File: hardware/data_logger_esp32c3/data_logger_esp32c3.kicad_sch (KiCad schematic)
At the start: 42 parts, among them U1 ESP32-C3-MINI-1, U3 LM321MF, U4 LM321MF, U5 LM321MF, U6 LM321MF, U7 LM321MF, U8 LM321MF

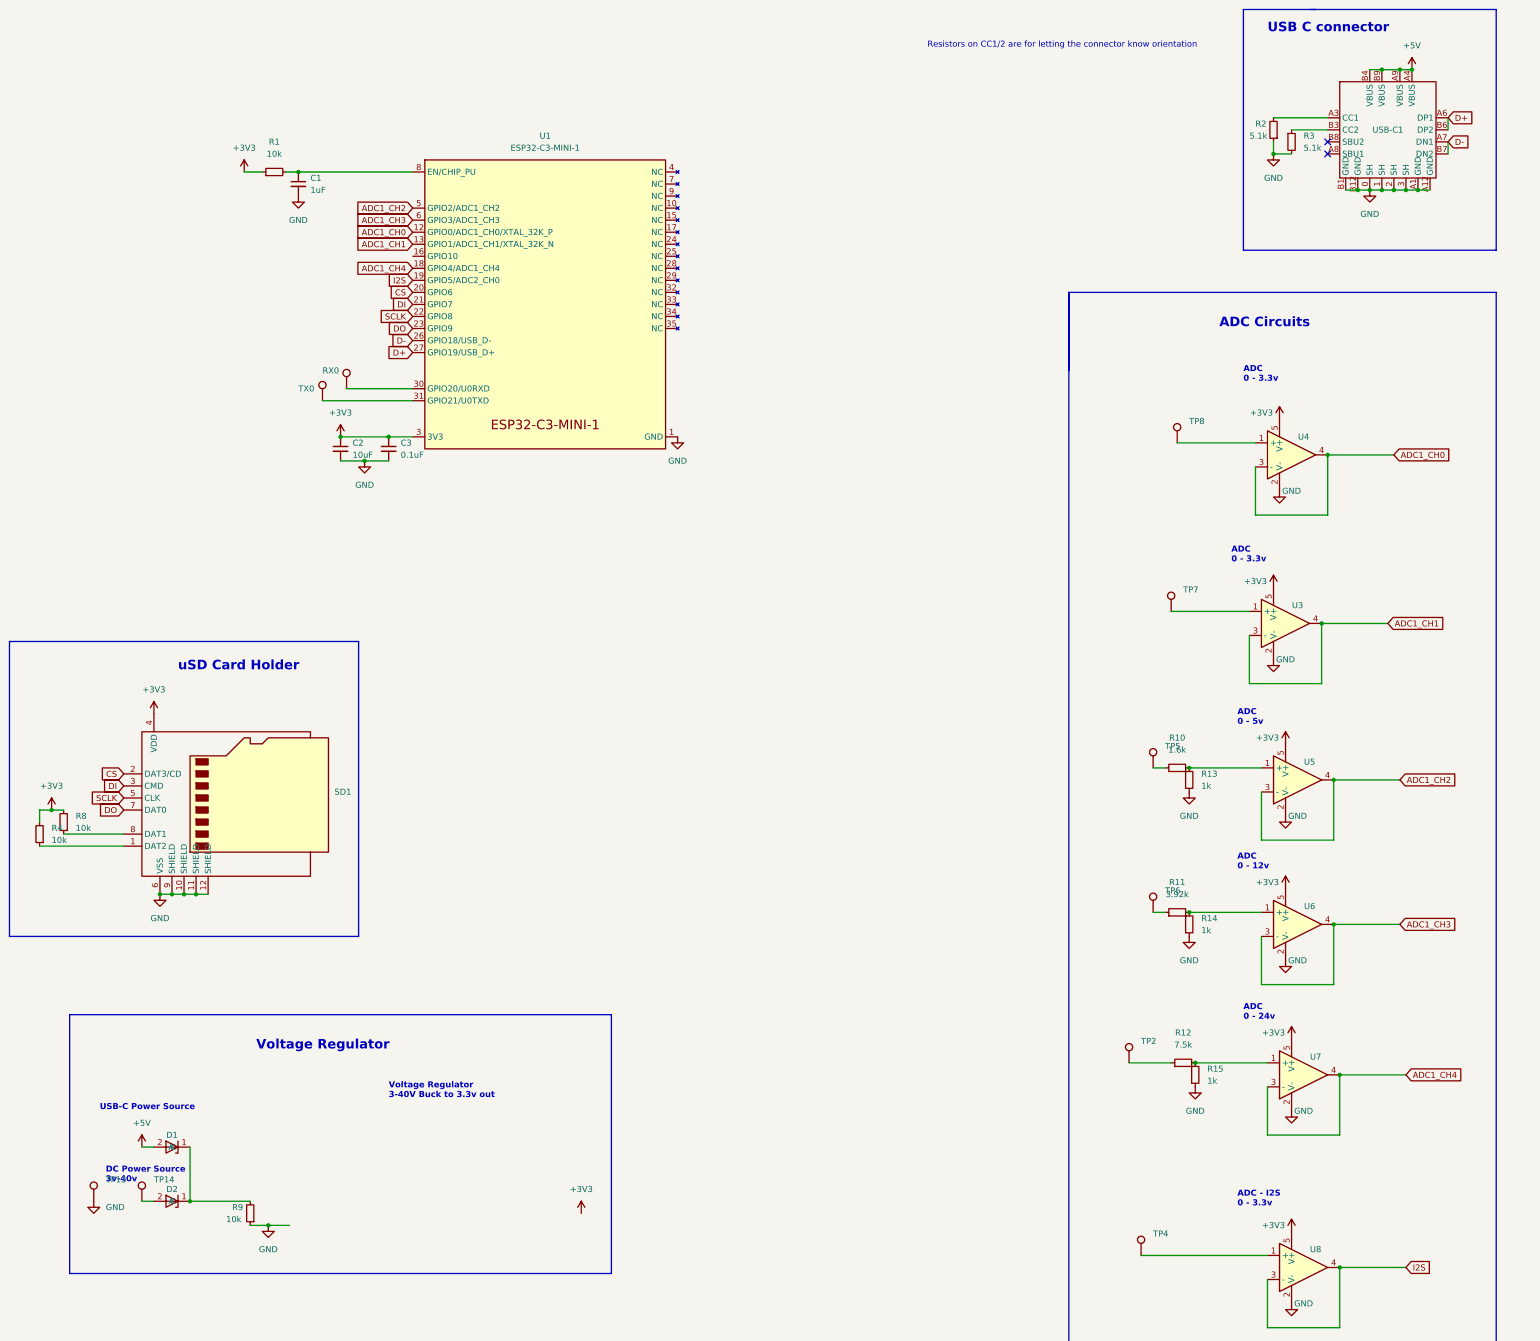
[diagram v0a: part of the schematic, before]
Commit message: added linear regulator, changed to 0402 passives
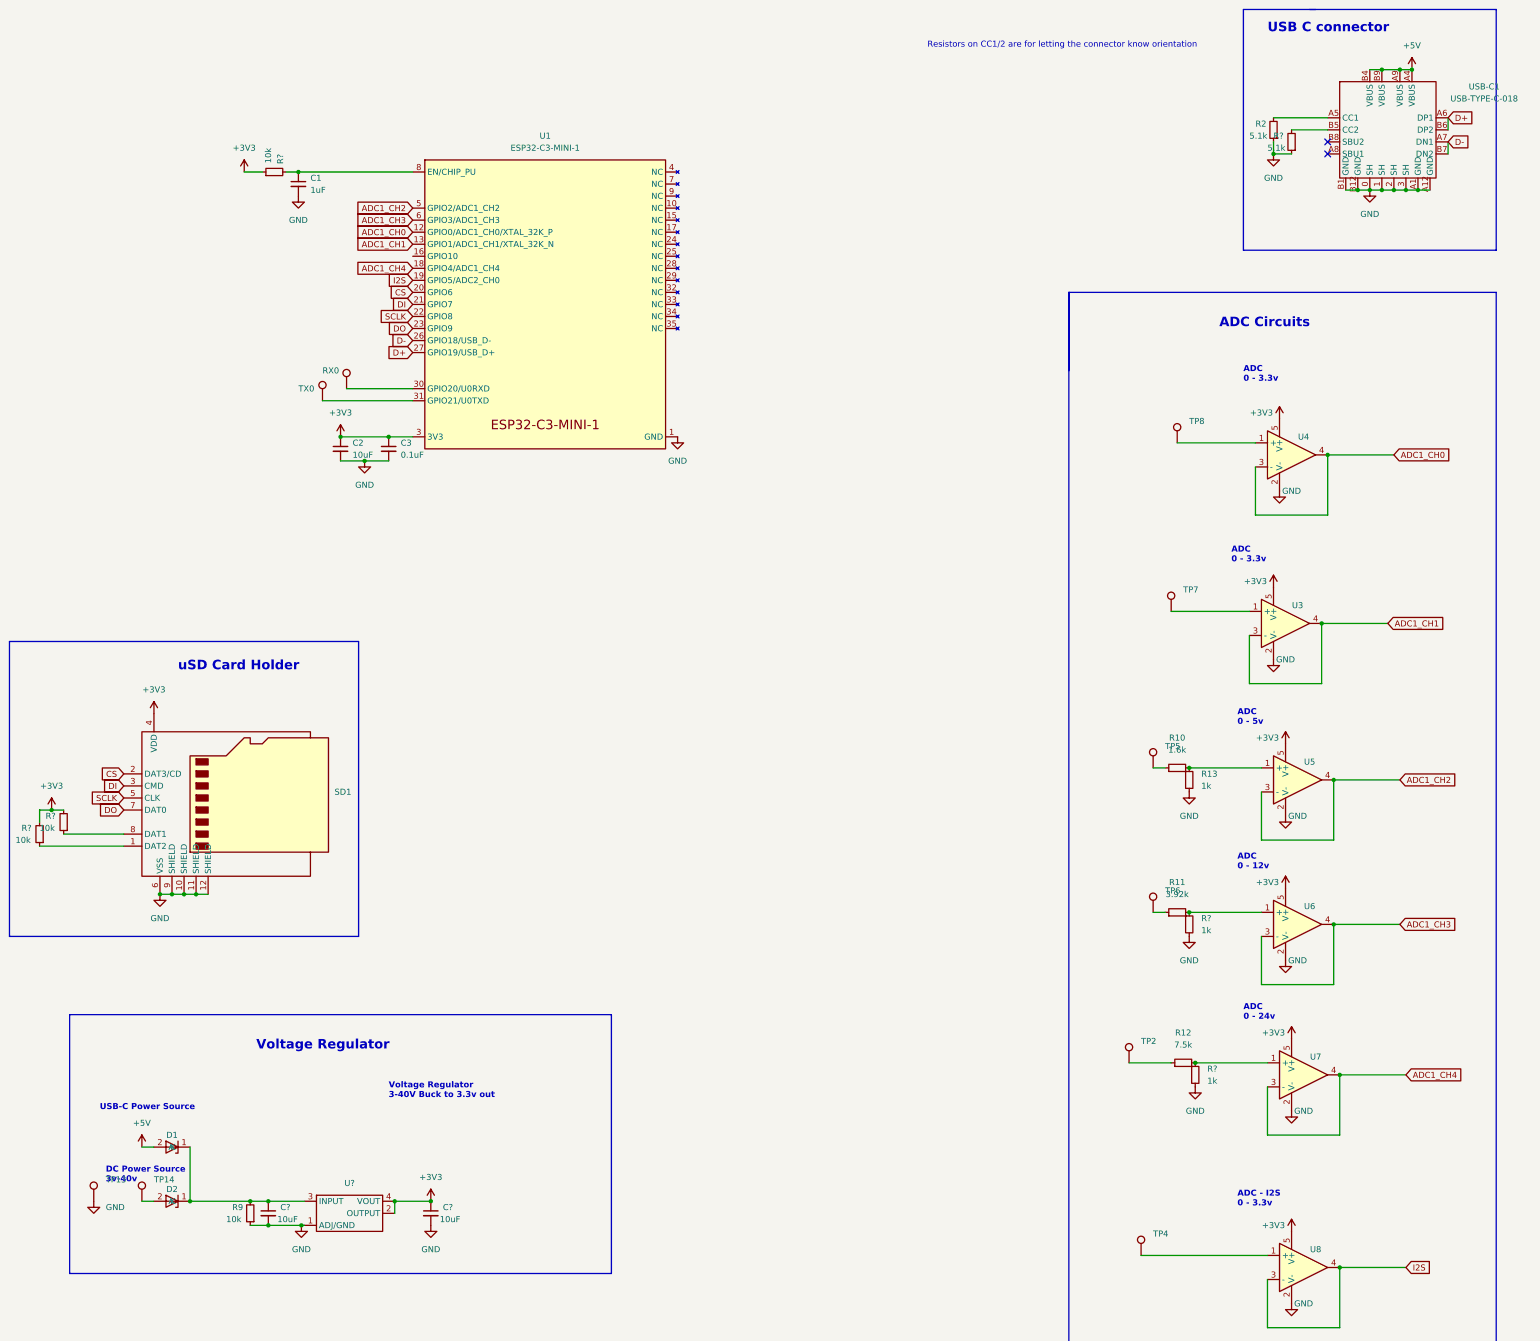
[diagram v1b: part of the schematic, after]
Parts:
- removed R1, R4, R8: 10k, Resistor_SMD:R_0603_1608Metric, symbol Device:R_Small
- removed R14, R15: 1k, Resistor_SMD:R_0603_1608Metric, symbol Device:R_Small
- removed R3: 5.1k, Resistor_SMD:R_0603_1608Metric, symbol Device:R_Small
- removed USB-C1: USB-TYPE-C-018, lib:USB-TYPE-C-018, symbol lib:USB-TYPE-C-018
- added C? (x2): 10uF, Capacitor_SMD:C_0603_1608Metric, symbol Device:C_Small
- added R? (x3): 10k, Resistor_SMD:R_0402_1005Metric, symbol Device:R_Small
- added R?: 5.1k, Resistor_SMD:R_0402_1005Metric, symbol Device:R_Small
- added R? (x2): 1k, Resistor_SMD:R_0402_1005Metric, symbol Device:R_Small
- added U?: AZ1117IH-3.3TRG1, symbol 1_project_specific:AZ1117IH-3.3TRG1
- added USB-C1: USB-TYPE-C-018, lib:USB-TYPE-C-018, symbol 1_project_specific:USB-TYPE-C-018
- R10: footprint Resistor_SMD:R_0603_1608Metric -> Resistor_SMD:R_0402_1005Metric; part_number RC-02W1601FT -> RMC04021.6K1%N
- R11: footprint Resistor_SMD:R_0603_1608Metric -> Resistor_SMD:R_0402_1005Metric; part_number ERJ3EKF3921V -> RC0402FR-073K9L
- R12: footprint Resistor_SMD:R_0603_1608Metric -> Resistor_SMD:R_0402_1005Metric; part_number C114634 -> AECR0402F7K50K9
- R13: footprint Resistor_SMD:R_0603_1608Metric -> Resistor_SMD:R_0402_1005Metric; part_number RS-03K102JT -> CR-02FL6----1K
- R2: footprint Resistor_SMD:R_0603_1608Metric -> Resistor_SMD:R_0402_1005Metric; part_number RC0603FR-075K1L -> ERJ2RKF5101X
- R9: footprint Resistor_SMD:R_0603_1608Metric -> Resistor_SMD:R_0402_1005Metric; part_number AC0603FR-0710KL -> ERJ2RKF1002X
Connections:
- net +3V3: now also C?.1, R?.1, R?.2, R?.2, U?.2 (OUTPUT), U?.4 (VOUT)
- net +5V: now also USB-C1.A4 (VBUS), USB-C1.A9 (VBUS), USB-C1.B4 (VBUS), USB-C1.B9 (VBUS)
- net D+: now also USB-C1.A6 (DP1), USB-C1.B6 (DP2)
- net D-: now also USB-C1.A7 (DN1), USB-C1.B7 (DN2)
- net GND: now also C?.2, C?.2, R?.1, R?.2, R?.2, U?.1 (ADJ/GND), USB-C1.0 (SH), USB-C1.1 (SH), USB-C1.2 (SH), USB-C1.3 (SH), USB-C1.A1 (GND), USB-C1.A12 (GND), USB-C1.B1 (GND), USB-C1.B12 (GND)
- net at R2.2: now also USB-C1.A5 (CC1)
- net at R12.2, U7.1 (+): now also R?.1
- net at D1.1 (K), D2.1 (K), R9.2: now also C?.1, U?.3 (INPUT)
- net at R11.2, U6.1 (+): now also R?.1
- net at SD1.1 (DAT2): now also R?.1
- net at SD1.8 (DAT1): now also R?.1
- net at C1.1, U1.8 (EN/CHIP_PU): now also R?.2
- new net: R?.2, USB-C1.B5 (CC2)

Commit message: Adding to pcb
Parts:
- removed C? (x2): 10uF, Capacitor_SMD:C_0603_1608Metric, symbol Device:C_Small
- removed D1, D2: B0530WS_SE, lib:B0530WS_SE, symbol lib:B0530WS_SE
- removed TP1, TP10, TP11, TP12, TP13, TP14, TP2, TP3, TP4, TP5, TP6, TP7, TP8, TP9: TestPoint, TestPoint:TestPoint_Loop_D2.50mm_Drill1.0mm, symbol Connector:TestPoint
- added 3V3, ADC1+1, ADC1-1, ADC2+1, ADC2-1, ADC3+1, ADC3-1, ADC4+1, ADC4-1, ADC5+1, ADC5-1, ADC6+1, ADC6-1, DC+1, DC-1, VIN1: TestPoint, TestPoint:TestPoint_THTPad_1.0x1.0mm_Drill0.5mm, symbol Connector:TestPoint
- added C4, C5: 10uF, Capacitor_SMD:C_0603_1608Metric, symbol Device:C_Small
- added D1: LTVS16H5.0T5G, 1_project_footprints:DFN1610, symbol 1_project_specific:LTVS16H5.0T5G
- added U10, U9: A03401A, 1_project_footprints:SOT-23, symbol 1_project_specific:A03401A
- C1: footprint Capacitor_SMD:C_0603_1608Metric -> Capacitor_SMD:C_0402_1005Metric; part_number TMK107AB7105KAHT -> 0402X105K6R3NT
- C2: part_number GRM188R61A106ME69D -> CL10A106KO8NQNC
- C3: footprint Capacitor_SMD:C_0603_1608Metric -> Capacitor_SMD:C_0402_1005Metric; part_number AC0603KRX7R9BB104 -> GCM155L81E104KE02D
- RX0, TX0: footprint TestPoint:TestPoint_Loop_D2.50mm_Drill1.0mm -> TestPoint:TestPoint_THTPad_1.0x1.0mm_Drill0.5mm
- SD1: footprint lib:472192001 -> 1_project_footprints:472192001
- U1: footprint Espressif:ESP32-C3-MINI-1 -> 1_espressif:ESP32-C3-MINI-1
- U2: renamed from U?; footprint (none) -> 1_project_footprints:SOT-223-4
- U3, U4, U5, U6, U7, U8: footprint lib:LM321MF -> 1_project_footprints:LM321MF
- USB-C1: footprint lib:USB-TYPE-C-018 -> 1_project_footprints:USB-TYPE-C-018
- gave numbers to parts that had none: 6
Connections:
- net +3V3: now also 3V3.1, C5.1
- net +5V: now also U10.3 (D)
- net GND: now also ADC1-1.1, ADC2-1.1, ADC3-1.1, ADC4-1.1, ADC5-1.1, ADC6-1.1, C4.2, C5.2, D1.2 (A), DC-1.1, U10.1 (G), U9.1 (G)
- net at U3.1 (+): now also ADC2+1.1
- net at R10.1: now also ADC3+1.1
- net at R11.1: now also ADC4+1.1
- net at U4.1 (+): now also ADC1+1.1
- net at R12.1: now also ADC5+1.1
- net at R9.2, U2.3 (INPUT): now also C4.1, U10.2 (S), U9.2 (S), VIN1.1
- net at U8.1 (+): now also ADC6+1.1
- new net: D1.1 (K), DC+1.1, U9.3 (D)
- no-connect marks 2 -> 3
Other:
- note added: "DC Source"
- note added: "Linear Voltage Regulator"
- note removed: "DC Power Source 3v-40v"
- note removed: "Voltage Regulator"
- note removed: "Voltage Regulator 3-40V Buck to 3.3v out"
- moved on the sheet: R10, R11, R12, R13, R5, R6, U4

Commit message: More hardware work
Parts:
- removed U1: ESP32-C3-MINI-1, 1_espressif:ESP32-C3-MINI-1, symbol Espressif:ESP32-C3-MINI-1
- added U1: ESP32-C3-MINI-1, 1_espressif:ESP32-C3-MINI-1, symbol 1_espressif:ESP32-C3-MINI-1
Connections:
- net +3V3: now also U1.3 (3V3)
- net ADC1_CH0: now also U1.12 (GPIO0/ADC1_CH0/XTAL_32K_P)
- net ADC1_CH1: now also U1.13 (GPIO1/ADC1_CH1/XTAL_32K_N)
- net ADC1_CH2: now also U1.5 (GPIO2/ADC1_CH2)
- net ADC1_CH3: now also U1.6 (GPIO3/ADC1_CH3)
- net ADC1_CH4: now also U1.18 (GPIO4/ADC1_CH4)
- net CS: now also U1.20 (GPIO6)
- net D+: now also U1.27 (GPIO19/USB_D+)
- net D-: now also U1.26 (GPIO18/USB_D-)
- net DI: now also U1.21 (GPIO7)
- net DO: now also U1.23 (GPIO9)
- net GND: now also U1.1 (GND), U1.11, U1.14, U1.2 (GND), U1.36 (GND), U1.37 (GND), U1.38 (GND), U1.39 (GND), U1.40 (GND), U1.41 (GND), U1.42 (GND), U1.43 (GND), U1.44 (GND), U1.45 (GND), U1.46 (GND), U1.47 (GND), U1.48 (GND), U1.49 (GND), U1.50 (GND), U1.51 (GND), U1.52 (GND), U1.53 (GND)
- net I2S: now also U1.19 (GPIO5/ADC2_CH0)
- net SCLK: now also U1.22 (GPIO8)
- net at C1.1, R4.2: now also U1.8 (EN/CHIP_PU)
- net at RX0.1: now also U1.30 (GPIO20/U0RXD)
- net at TX0.1: now also U1.31 (GPIO21/U0TXD)
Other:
- note added: "MCU"
- note removed: "Resistors on CC1/2 are for letting the connector know orientation"

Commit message: adding to hardware
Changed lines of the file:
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@@
-    (pin "1")
-  )
-  (symbol (lib_id "Connector:TestPoint") (at 50.8 270.51 0) (unit 1)
-    (in_bom yes) (on_board yes)
-    (property "Reference" "DC+1" (id 0) (at 50.8 265.43 0)
-      (effects (font (size 1.27 1.27)) (justify left))
-    )
-    (property "Value" "TestPoint" (id 1) (at 53.34 268.4779 0)
-      (effects (font (size 1.27 1.27)) (justify left) hide)
-    )
-    (property "Footprint" "TestPoint:TestPoint_THTPad_1.0x1.0mm_Drill0.5mm" (id 2) (at 55.88 270.51 0)
-      (effects (font (size 1.27 1.27)) hide)
-    )
-    (property "Datasheet" "~" (id 3) (at 55.88 270.51 0)
-      (effects (font (size 1.27 1.27)) hide)
-    )
     (pin "1")
   )
@@
     (pin "1")
   )
+  (symbol (lib_id "Connector:TestPoint") (at 468.63 238.125 0) (unit 1)
+    (in_bom yes) (on_board yes)
+    (property "Reference" "ADC5-1" (id 0) (at 467.995 232.41 0)
+      (effects (font (size 1.27 1.27)) (justify left))
+    )
+    (property "Value" "TestPoint" (id 1) (at 471.17 236.0929 0)
+      (effects (font (size 1.27 1.27)) (justify left) hide)
+    )
+    (property "Footprint" "TestPoint:TestPoint_THTPad_1.0x1.0mm_Drill0.5mm" (id 2) (at 473.71 238.125 0)
+      (effects (font (size 1.27 1.27)) hide)
+    )
+    (property "Datasheet" "~" (id 3) (at 473.71 238.125 0)
+      (effects (font (size 1.27 1.27)) hide)
+    )
+    (pin "1")
+  )
   (symbol (lib_id "Connector:TestPoint") (at 40.64 270.51 0) (unit 1)
     (in_bom yes) (on_board yes)
-    (property "Reference" "DC-1" (id 0) (at 39.37 265.43 0)
+    (property "Reference" "DC-1" (id 0) (at 40.005 265.43 0)
       (effects (font (size 1.27 1.27)) (justify left))
     )
@@
     )
     (property "Datasheet" "~" (id 3) (at 45.72 270.51 0)
-      (effects (font (size 1.27 1.27)) hide)
-    )
-    (pin "1")
-  )
-  (symbol (lib_id "Connector:TestPoint") (at 468.63 238.125 0) (unit 1)
-    (in_bom yes) (on_board yes)
-    (property "Reference" "ADC5-1" (id 0) (at 467.995 232.41 0)
-      (effects (font (size 1.27 1.27)) (justify left))
-    )
-    (property "Value" "TestPoint" (id 1) (at 471.17 236.0929 0)
-      (effects (font (size 1.27 1.27)) (justify left) hide)
-    )
-    (property "Footprint" "TestPoint:TestPoint_THTPad_1.0x1.0mm_Drill0.5mm" (id 2) (at 473.71 238.125 0)
-      (effects (font (size 1.27 1.27)) hide)
-    )
-    (property "Datasheet" "~" (id 3) (at 473.71 238.125 0)
       (effects (font (size 1.27 1.27)) hide)
     )
@@
     (pin "1")
   )
+  (symbol (lib_id "Connector:TestPoint") (at 50.8 270.51 0) (unit 1)
+    (in_bom yes) (on_board yes)
+    (property "Reference" "DC+1" (id 0) (at 50.165 265.43 0)
+      (effects (font (size 1.27 1.27)) (justify left))
+    )
+    (property "Value" "TestPoint" (id 1) (at 53.34 268.4779 0)
+      (effects (font (size 1.27 1.27)) (justify left) hide)
+    )
+    (property "Footprint" "TestPoint:TestPoint_THTPad_1.0x1.0mm_Drill0.5mm" (id 2) (at 55.88 270.51 0)
+      (effects (font (size 1.27 1.27)) hide)
+    )
+    (property "Datasheet" "~" (id 3) (at 55.88 270.51 0)
+      (effects (font (size 1.27 1.27)) hide)
+    )
+    (pin "1")
+  )
   (symbol (lib_id "power:GND") (at 509.27 116.84 0) (unit 1)
     (in_bom yes) (on_board yes)
@@
       (reference "D1") (unit 1) (value "LTVS16H5.0T5G") (footprint "1_project_footprints:DFN1610")
     )
-    (path "/4b2a0f39-8828-4267-950c-fe5adc6b96ac"
+    (path "/ca03cb07-5523-4de3-accf-b5e1342ff21a"
       (reference "DC+1") (unit 1) (value "TestPoint") (footprint "TestPoint:TestPoint_THTPad_1.0x1.0mm_Drill0.5mm")
     )
-    (path "/b8114865-64b9-4b79-b52d-fcdd217c92d8"
+    (path "/bbe5e08f-c4ee-43f4-9366-05d99dc3ae4e"
       (reference "DC-1") (unit 1) (value "TestPoint") (footprint "TestPoint:TestPoint_THTPad_1.0x1.0mm_Drill0.5mm")
     )

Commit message: Add gpio expander.  Layout complete
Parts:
- removed ADC2+1, ADC2-1: TestPoint, TestPoint:TestPoint_THTPad_1.0x1.0mm_Drill0.5mm, symbol Connector:TestPoint
- removed U3: LM321MF, 1_project_footprints:LM321MF, symbol lib:LM321MF
- added C6, C7: 0.1uF, Capacitor_SMD:C_0402_1005Metric, symbol Device:C_Small
- added I2C_SCL1, I2C_SDA1, IO0, IO1, IO10, IO11, IO12, IO13, IO14, IO15, IO2, IO3, IO4, IO5, IO6, IO7, IO8, IO9, NINT1, NRESET1: TestPoint, TestPoint:TestPoint_THTPad_1.0x1.0mm_Drill0.5mm, symbol Connector:TestPoint
- added R14, R15: 10k, Resistor_SMD:R_0402_1005Metric, symbol Device:R_Small
- added R16, R8: 4.7k, Resistor_SMD:R_0402_1005Metric, symbol Device:R_Small
- added U11: SX1509BIULTRT, 1_project_footprints:QFN-28-EP(4x4), symbol 1_project_specific:SX1509BIULTRT
- U1: footprint 1_espressif:ESP32-C3-MINI-1 -> Espressif:ESP32-C3-MINI-1
- USB-C1: footprint 1_project_footprints:USB-TYPE-C-018 -> lib:USB-TYPE-C-018
- renumbered ADC1-1 to A0N1, ADC1+1 to A0P1, ADC3-1 to A2N1, ADC3+1 to A2P1, ADC4-1 to A3N1, ADC4+1 to A3P1, ADC5-1 to A4N1, ADC5+1 to A4P1, ADC6-1 to I2SN1, ADC6+1 to I2SP1
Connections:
- net +3V3: now also C6.1, C7.1, R14.2, R15.2, R16.2, R8.2, U11.18 (VCC2), U11.4 (VCC1)
- net GND: now also C6.2, C7.2, U11.10 (ADDR1), U11.17 (GND), U11.26 (ADDR0), U11.29 (PAD), U11.3 (GND)
- net I2C_SCL: now reaches U1.16 (GPIO10)
- net I2C_SCL: now also I2C_SCL1.1, R8.1, U11.25 (SCL)
- net ADC1_CH1 renamed I2C_SDA
- net I2C_SDA: now also I2C_SDA1.1, R16.1, U11.24 (SDA)
- new net: IO15.1, U11.22 (IO15)
- new net: IO1.1, U11.28 (IO1)
- new net: IO11.1, U11.16 (IO11)
- new net: IO5.1, U11.6 (IO5)
- new net: IO14.1, U11.21 (IO14)
- new net: IO7.1, U11.8 (IO7)
- new net: IO6.1, U11.7 (IO6)
- new net: IO13.1, U11.20 (IO13)
- new net: IO3.1, U11.2 (IO3)
- new net: IO2.1, U11.1 (IO2)
- new net: IO8.1, U11.13 (IO8)
- new net: IO9.1, U11.14 (IO9)
- new net: IO10.1, U11.15 (IO10)
- new net: IO12.1, U11.19 (IO12)
- new net: IO0.1, U11.27 (IO0)
- new net: IO4.1, U11.5 (IO4)
- new net NINT: NINT1.1, R15.1, U11.9 (NINT)
- new net NRESET: NRESET1.1, R14.1, U11.23 (NRESET)
- no-connect marks 3 -> 2
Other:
- note added: "GPIO Expander"
- moved on the sheet: A0N1, A0P1, I2SN1, U4

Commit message: Edit schematic
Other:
- moved on the sheet: A0N1, A0P1, A2N1, A2P1, A3N1, A3P1, A4N1, A4P1, C1, C2, C3, C6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
